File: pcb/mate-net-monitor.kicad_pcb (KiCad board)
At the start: 2 copper layers, 65 parts, among them J1 RJHSE-5081, J2 Conn_02x04_Odd_Even, J3 Conn_02x02_Odd_Even, J4 6P6C, J5 6P6C, Q1 Si2337DS, U1 LM5085MY, U2 TLP185, U3 TLP185, U4 TLP185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

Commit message: layout P1
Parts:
- removed the J2 at (114.3, 72.4)
- removed R15: 0, Resistor_SMD:R_0805_2012Metric
- added J4: Conn_01x08, Connector_PinSocket_2.54mm:PinSocket_1x08_P2.54mm_Vertical, F.Cu at (123.2, 72.4)
- C9: value ?uF -> 180uF; footprint Capacitor_SMD:CP_Elec_4x4.5 -> Capacitor_SMD:CP_Elec_6.3x5.9
- R4, R7, R8, R9: value 22 -> 47k
- moved C7 62.1 mm to (152.7, 77.0), turned to 270 degrees
- moved C8 55.5 mm to (149.9, 77.0), turned to 270 degrees
- moved D3 35.8 mm to (120.3, 109.1), turned to 90 degrees
- moved D5 33.9 mm to (128.5, 83.1), turned to 90 degrees
- moved R9 33.7 mm to (147.3, 88.8), turned to 270 degrees
- moved D2 33.6 mm to (117.5, 109.1), turned to 90 degrees
- moved R4 32.9 mm to (154.9, 88.8), turned to 270 degrees
- moved D1 31.5 mm to (114.7, 109.1), turned to 90 degrees
- moved R8 31.3 mm to (149.9, 88.8), turned to 270 degrees
- moved R7 28.5 mm to (152.4, 88.8), turned to 270 degrees
- moved R5 27.2 mm to (136.8, 104.9), turned to 180 degrees
- moved R3 26.5 mm to (139.1, 85.0), turned to 270 degrees
- moved C4 26.2 mm to (136.5, 81.2), turned to 90 degrees
- moved C1 20.9 mm to (124.5, 104.4)
- moved R17 19.6 mm to (135.9, 76.3), turned to 270 degrees
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- renumbered J4 to J1, J5 to J2, J1 to J5
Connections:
- net Net-(C3-Pad2) renamed /P5V_VCC
- net Net-(C4-Pad2) renamed /P5V_ADJ
- net Net-(C5-Pad1) renamed /P5V_AC
- net Net-(D5-Pad1) renamed /P5V_SW
- net Net-(Q1-Pad1) renamed /P5V_PGATE
- net Net-(R23-Pad2) renamed /U5_EN
- A1 pad RST: (no net) -> Net-(A1-PadRST)
- A1 pad VUSB: Net-(A1-PadVUSB) -> +5V
- H3 pad 1: GND -> Net-(H3-Pad1)
- H4 pad 1: GND -> Net-(H4-Pad1)
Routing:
- net +3V3: track 0.00 -> 147.2 mm, vias 0 -> 3
- net GND: track 0.00 -> 69.6 mm, vias 0 -> 39
- net /MAG_NET_GND: track 0.00 -> 63.9 mm
- net +BATT: track 0.00 -> 58.3 mm
- net /MAG_NET_P14V: track 0.00 -> 55.7 mm
- net +5V: track 0.00 -> 51.0 mm
- net /PB_UART1_RX: track 0.00 -> 43.2 mm, vias 0 -> 1
- net /MATE_NET_TXD: track 0.00 -> 40.9 mm
- net /PB_UART2_TX: track 0.00 -> 37.3 mm
- net /PB_D3: track 0.00 -> 34.6 mm, vias 0 -> 2
- net /PB_D2: track 0.00 -> 33.5 mm
- net /MAG_NET_A: track 0.00 -> 32.4 mm
- net /CONN_ADC1: track 0.00 -> 32.0 mm, vias 0 -> 1
- net /PB_UART1_TX: track 0.00 -> 31.2 mm, vias 0 -> 1
- net /CONN_ADC2: track 0.00 -> 28.4 mm, vias 0 -> 1
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- added copper zone on F.Cu, net +5V
- added copper zone on F.Cu, net +BATT
- added copper zone on F.Cu, net /P5V_ISEN
- added copper zone on F.Cu, net /P5V_SW
- added copper zone on F.Cu, net /PBATT_CONN
- added copper zone on B.Cu, net GND
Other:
- board outline added: 74.7 x 51.4 mm
- net class 6/6 added: clearance 0.1524, trace_width 0.1524, via_dia 0.6096, via_drill 0.3048
- net class 8/6 added: clearance 0.1524, trace_width 0.2032, via_dia 0.6096, via_drill 0.3048
- net class Default: clearance 0.2 -> 0.2032; trace_width 0.25 -> 0.2032; via_dia 0.8 -> 0.6096; via_drill 0.4 -> 0.3048
- rule trace_clearance: 0.2 -> 0.2032
- rule trace_min: 0.2 -> 0.1524
- rule via_min_size: 0.4 -> 0.3048
- board text added: "Caution! 24-60VDC"
- board text added: "Intentionally"
- board text added: "Inverter"
- board text added: "Left Blank"
- board text added: "MATE Net"
- board text added: "MATE Net Monitor ICH ENB 2021 Morton’s Point Camp"
- board text added: "Mag Remote"
- board text added: "This Space"

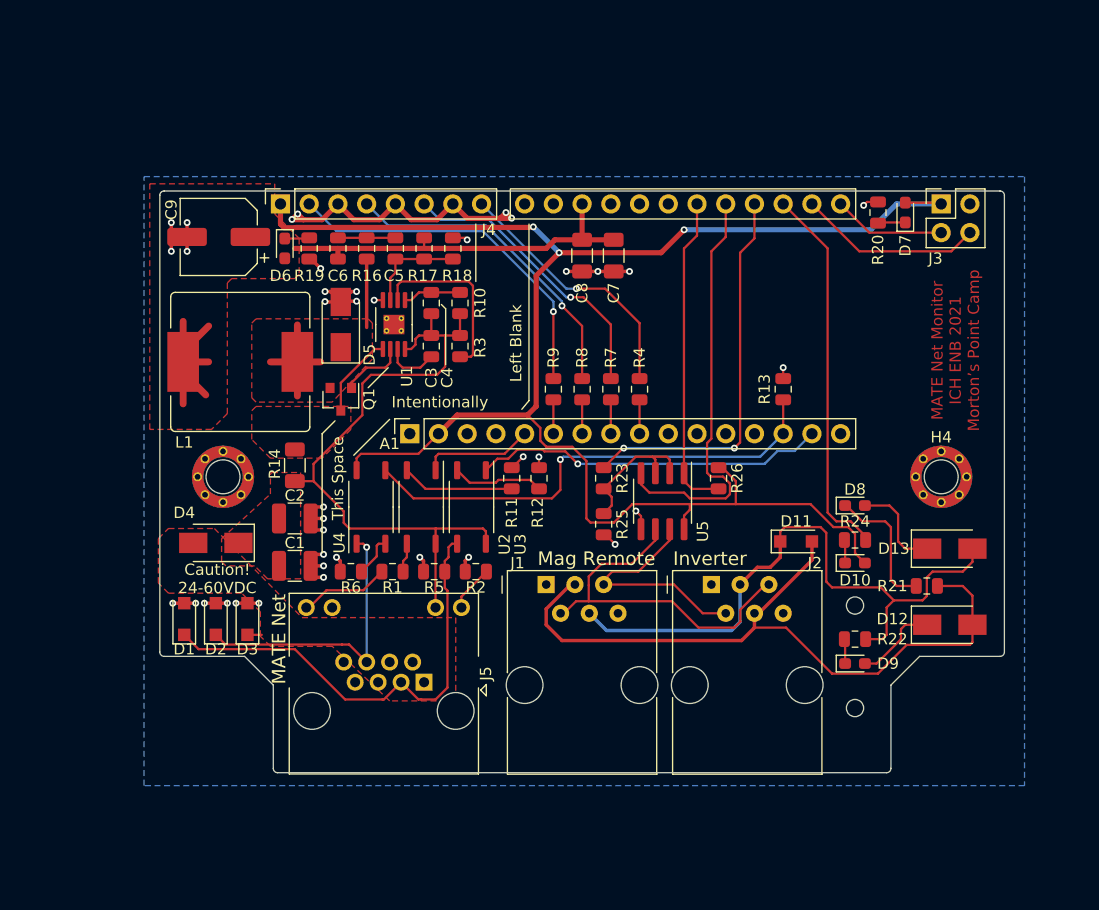
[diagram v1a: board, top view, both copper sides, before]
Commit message: layout P1 schematic P1
review and fix circuits before fab
* fix Q1 D/S orientation
* fix J1/J2 labels to match pin usage
* add 3d models RJ45, RJ12, Boron, inductor
* new gerbers and pdfs
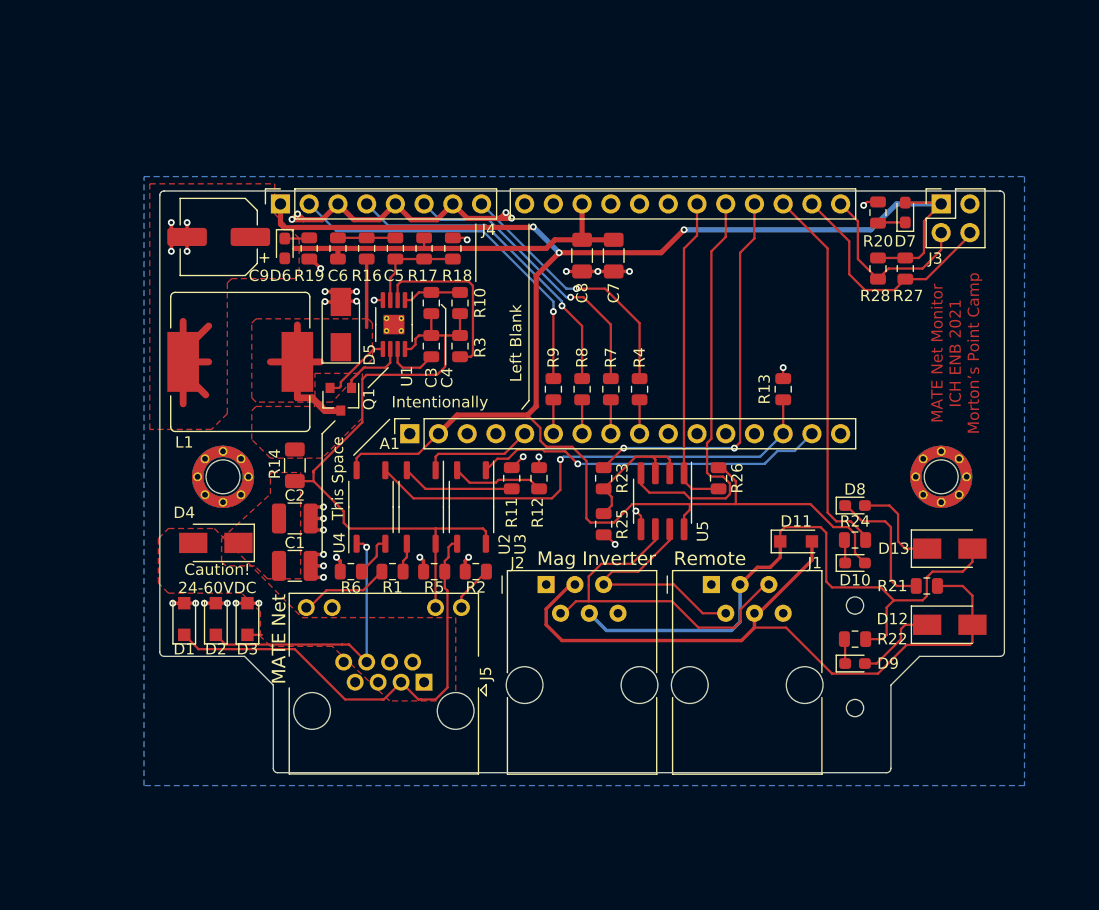
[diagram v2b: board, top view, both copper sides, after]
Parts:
- added R27: 4.7k-DNP, Resistor_SMD:R_0805_2012Metric, F.Cu at (178.4, 78.1)
- added R28: 4.7k-DNP, Resistor_SMD:R_0805_2012Metric, F.Cu at (176.0, 78.1)
- C1, C2: value 1uF -> 3.3uF
- R3: value 133k -> 118k
- renumbered J2 to J1, J1 to J2
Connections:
- Q1 pad 2: /P5V_SW -> /P5V_ISEN
- Q1 pad 3: /P5V_ISEN -> /P5V_SW
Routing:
- net +3V3: track 147.2 -> 156.4 mm
- net /PB_SDA: track 9.94 -> 16.2 mm
- net /PB_SCL: track 16.4 -> 21.1 mm
- net /P5V_SW: track 16.8 -> 21.2 mm
- net /P5V_ISEN: track 7.41 -> 6.32 mm
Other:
- board text added: "Mag Inverter"
- board text added: "Remote"
- board text removed: "Inverter"
- board text removed: "Mag Remote"

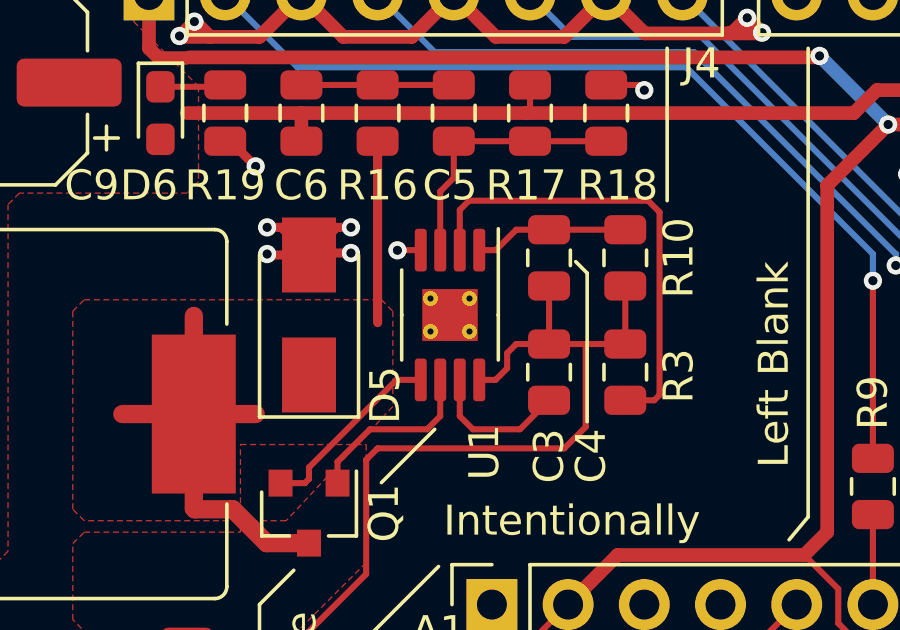
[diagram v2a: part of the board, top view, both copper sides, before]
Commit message: layout P1.1 update U1 footprint to have 0.3mm vias
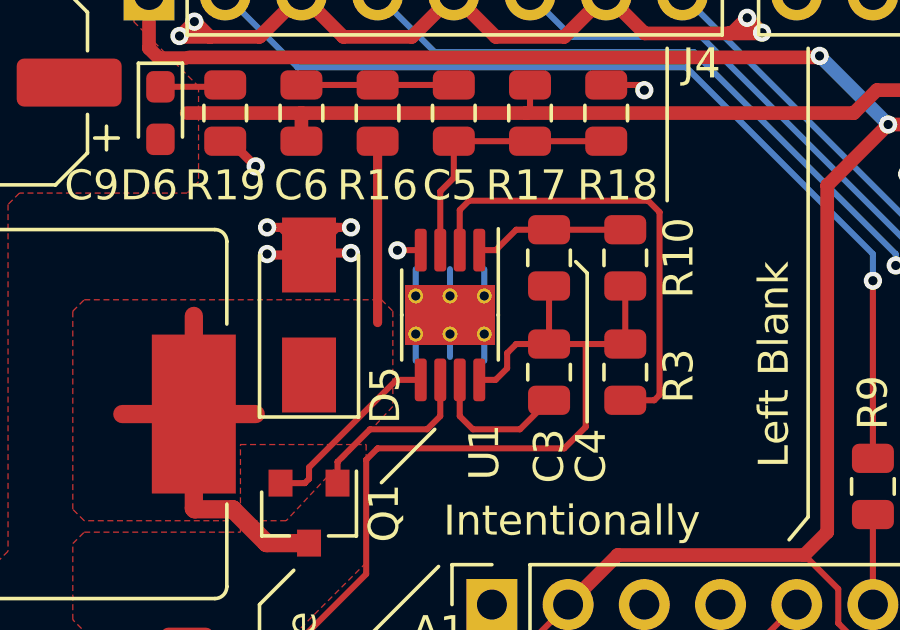
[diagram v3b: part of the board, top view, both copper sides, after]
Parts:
- U1: footprint Package_SO:MSOP-8-1EP_3x3mm_P0.65mm_EP1.73x1.85mm_ThermalVias -> mate-net-monitor-special:MSOP-8-1EP_3x3mm_P0.65mm_EP1.88x2mm_ThermalVias0.3mm
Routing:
- net GND: track 69.6 -> 76.0 mm
